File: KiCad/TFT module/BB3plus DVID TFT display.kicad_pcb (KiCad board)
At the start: 2 copper layers, 136 x 92 mm, 66 parts, among them IC1 TFP401APZP, IC2 TCA9554APWR, IC3 TSC2007IPWR, IC4 TPS61169DCKR, SW1 B3FS-4052P, SW2 B3FS-4052P, SW3 B3FS-4052P, SW4 B3FS-4052P, X1 5051102091, X2 F32D-1A7Y1-21040, X3 F3311A7H121006E200

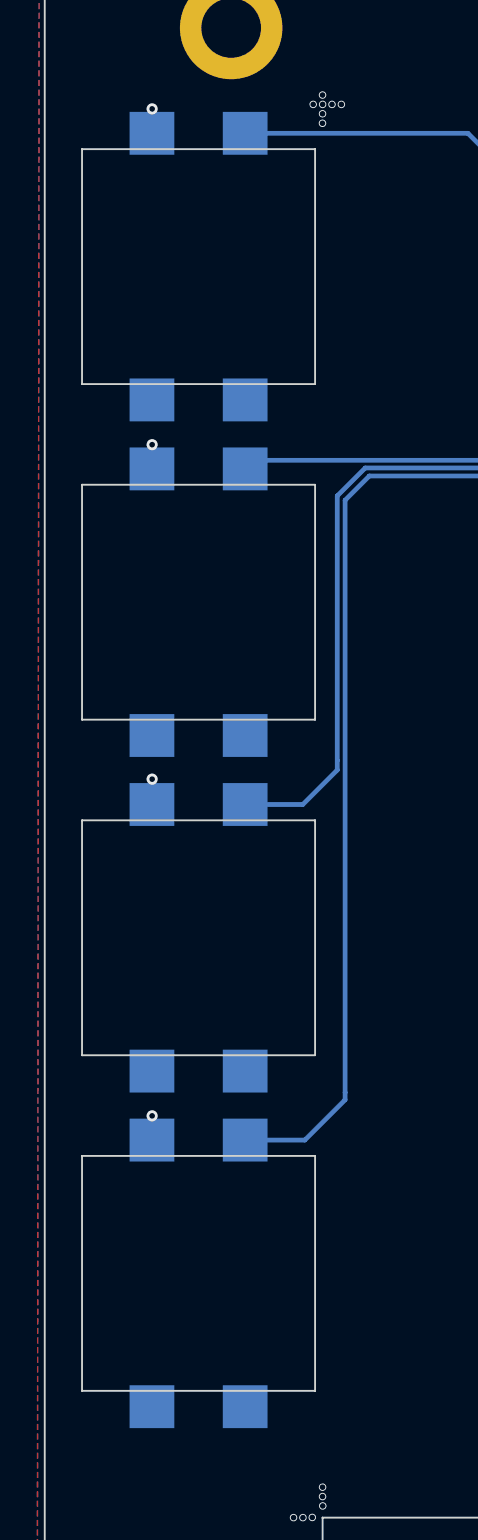
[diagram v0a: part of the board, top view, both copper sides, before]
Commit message: TFT display tactile switches footprint correction
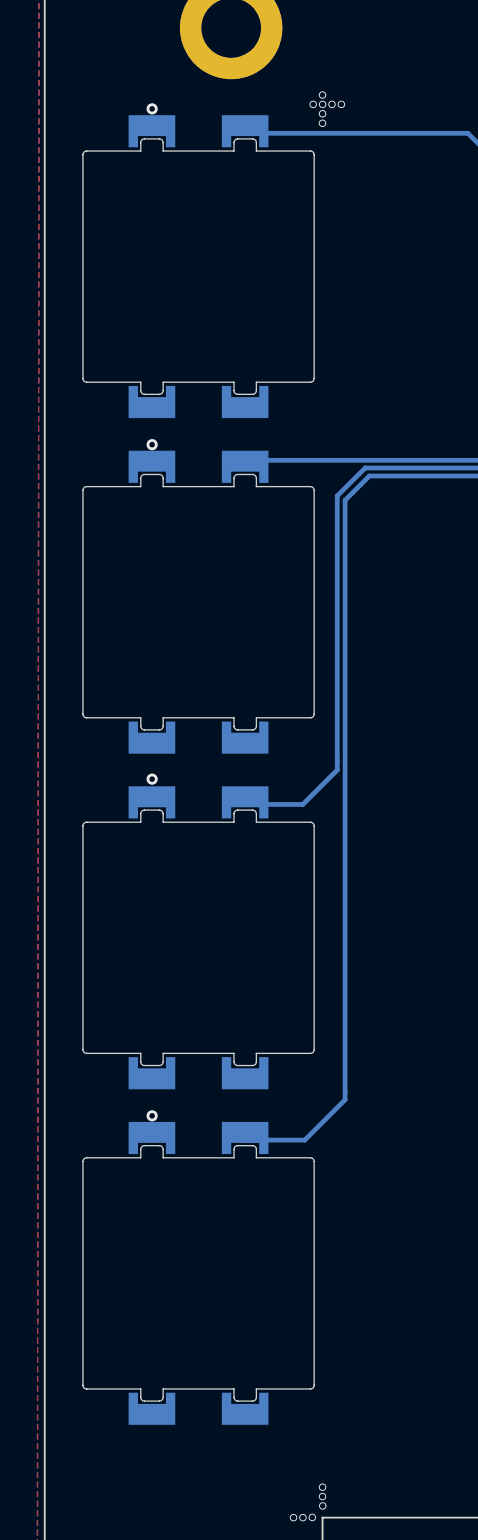
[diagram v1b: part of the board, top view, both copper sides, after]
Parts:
- SW1, SW2, SW3, SW4: footprint PCM_EEZ_unsorted:B3FS-4052P -> PCM_EEZ_unsorted:B3FS-4052P (cut out)
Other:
- outline, holes or cut-outs redrawn
- board text added: "${project_name} (12/2025 ${project_version})"
- board text removed: "${project_name} (11/2025 ${project_version})"

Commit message: Enclosure front and rear panel update, projects location reorganized
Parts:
- X1: value 5051102091 -> 5051102291
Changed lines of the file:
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@@
 			)
 		)
-		(model "${KICAD7_3RD_PARTY}/3dmodels/com_github_eez-open_eez-kicad-libraries/ER-TFT050-6.STEP"
+		(model "${KICAD7_3RD_PARTY}/3dmodels/com_github_eez-open_eez-kicad-libraries/ER-TFT050-6 (simplified).step"
 			(offset
 				(xyz 65.2 42 1)
@@
 			)
 		)
-		(property "Value" "5051102091"
+		(property "Value" "5051102291"
 			(at 0 0 0)
 			(unlocked yes)

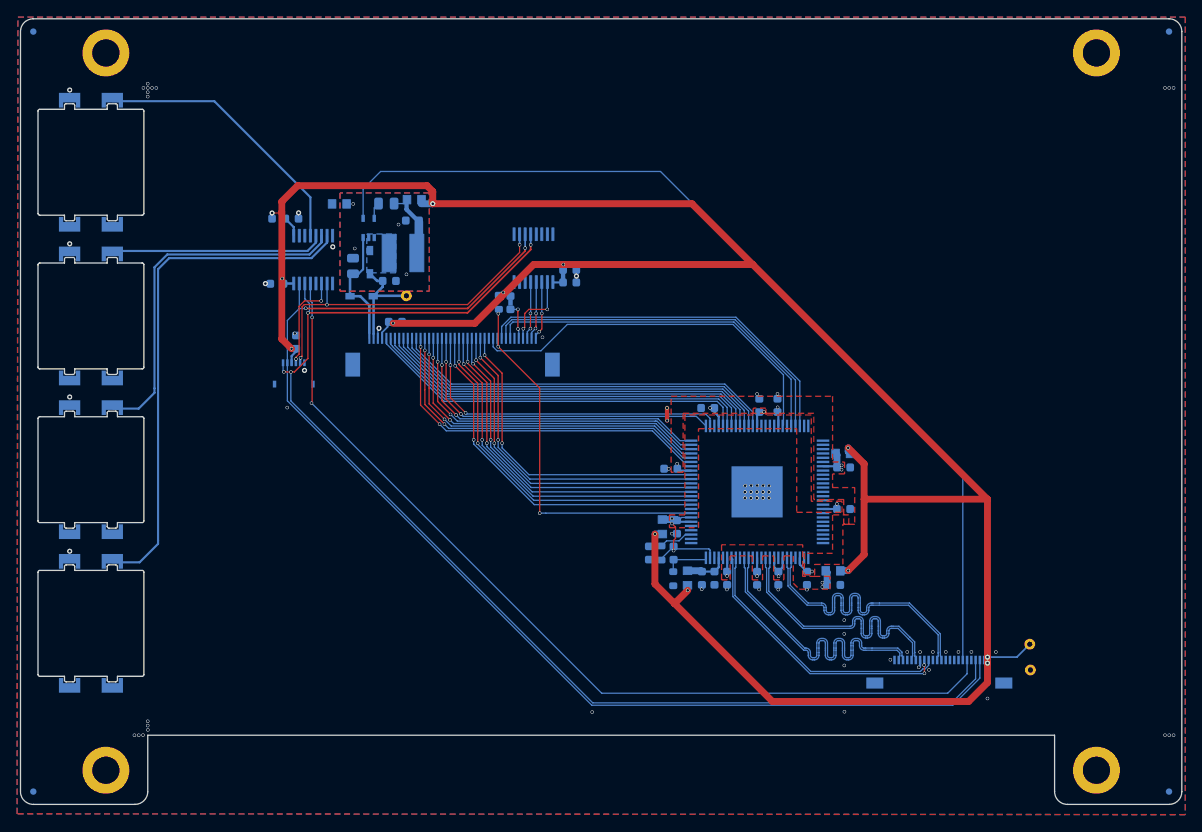
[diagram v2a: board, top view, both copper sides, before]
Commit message: EDID EEPROM added on TFT module
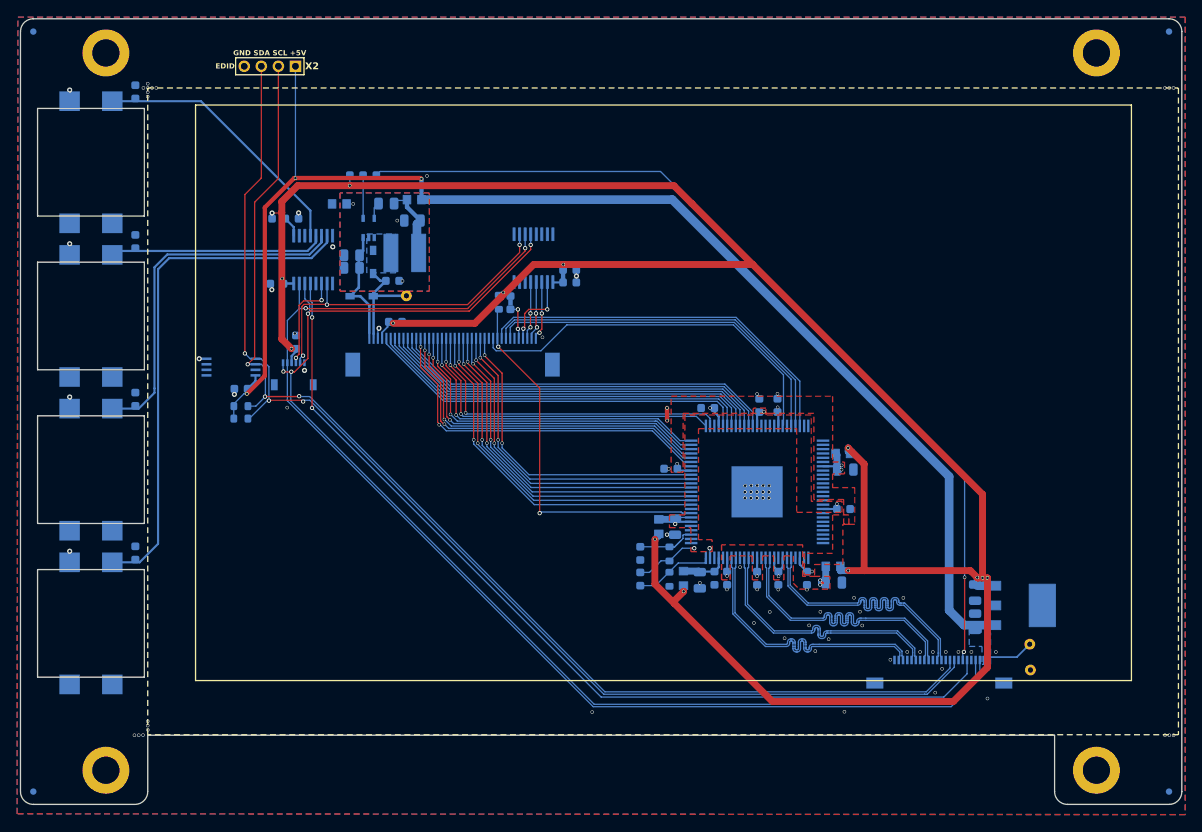
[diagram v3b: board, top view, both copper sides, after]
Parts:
- added C15: 10u, PCM_EEZ_passives:C_0805_2012Metric, B.Cu at (196.8, 120.1)
- added C16: 100n, PCM_EEZ_passives:C_0603_1608Metric, B.Cu at (110.8, 92.8)
- added C19: 10u, PCM_EEZ_passives:C_0805_2012Metric, B.Cu at (196.8, 116.7)
- added C22: 10n, PCM_EEZ_passives:C_0603_1608Metric, B.Cu at (98.5, 112.1)
- added C24: 10n, PCM_EEZ_passives:C_0603_1608Metric, B.Cu at (98.5, 94.0)
- added C25: 10n, PCM_EEZ_passives:C_0603_1608Metric, B.Cu at (98.5, 58.1)
- added C26: 10n, PCM_EEZ_passives:C_0603_1608Metric, B.Cu at (98.5, 75.6)
- added IC2: M24C04-RDW6TP, PCM_EEZ_SMD:TSSOP-8, B.Cu at (109.6, 90.3)
- added IC3: AZ1117CH2-3.3TRG1, PCM_EEZ_SMD:SOT223, B.Cu at (202.1, 118.2)
- added JP5: 0R, PCM_EEZ_SMD:JP3 shorted with 0R (0603), B.Cu at (125.9, 67.8)
- added R3: 10K, PCM_EEZ_passives:R_0603_1608Metric, B.Cu at (110.8, 94.9)
- added R4: 10K, PCM_EEZ_passives:R_0603_1608Metric, B.Cu at (110.8, 96.3)
- added R8: 9R1, Resistor_SMD:R_0805_2012Metric, B.Cu at (123.8, 78.7)
- added X2: M22-2010446, PCM_EEZ_connectors:M22-2010446, F.Cu at (114.2, 55.1)
- C1, C2, C3, C4: footprint PCM_EEZ_passives:C_0603_1608Metric -> PCM_EEZ_passives:C_0805_2012Metric
- C21: renamed from C18; footprint PCM_EEZ_passives:C_0603_1608Metric -> PCM_EEZ_passives:C_0805_2012Metric
- JP4: value ~ -> 0R
- SW1, SW2, SW3, SW4: footprint PCM_EEZ_unsorted:B3FS-4052P (cut out) -> PCM_EEZ_unsorted:B3FS-4052P
- X1: value 5051102291 -> 5051102091
- moved JP1 4.94 mm to (157.6, 115.1)
- moved R7 1.26 mm to (123.8, 77.2), turned to 0 degrees
- moved JP2 1.02 mm to (157.6, 112.1)
- moved R1 0.95 mm to (161.0, 112.2)
- moved FB3 0.53 mm to (180.2, 113.6)
- moved FB4 0.47 mm to (162.6, 115.0)
- moved R2 0.44 mm to (161.0, 115.1)
- moved FB1 0.42 mm to (159.8, 109.0)
- moved C28 0.37 mm to (128.6, 80.2)
- moved D1 0.37 mm to (126.3, 78.0)
- moved C4 0.35 mm to (164.6, 115.2)
- moved C2 0.32 mm to (181.6, 102.3)
- moved C3 0.28 mm to (180.2, 115.5)
- moved C1 0.24 mm to (161.7, 109.0)
- moved L1 0.21 mm to (130.0, 76.9)
- renumbered C15 to C17, C16 to C18, C17 to C20, C19 to C23, C20 to C27, C21 to C28, FM3 to FM2, FM2 to FM3, IC2 to IC4, IC3 to IC5, IC4 to IC6, R3 to R5, R4 to R6, R5 to R7, TP2 to TP1, TP1 to TP2, X2 to X3, X3 to X4
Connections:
- FB5 pad 1: +3V3 -> +5V
- IC6 pad 4: /BL_PWM -> Net-(IC6-CTRL)
- TP2 pad 1: +3V3 -> +5V
- X1 pad 1: +3V3 -> +5V
- X1 pad 14: /DSI_CLK_P -> /DSI_D1_P
- X1 pad 15: /DSI_CLK_N -> /DSI_D1_N
- X1 pad 17: /DSI_D1_P -> /DSI_D0_P
- X1 pad 18: /DSI_D1_N -> /DSI_D0_N
- X1 pad 20: /DSI_D0_P -> /DSI_CLK_P
- X1 pad 21: /DSI_D0_N -> /DSI_CLK_N
- X1 pad 8: unconnected-(X1-DPHY_D3_P-Pad8) -> /EDID_SDA
- X1 pad 9: unconnected-(X1-DPHY_D3_N-Pad9) -> /EDID_SCL
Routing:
- net +5V: track 0.00 -> 165.8 mm, vias 0 -> 3
- net /EDID_SDA: track 0.00 -> 142.1 mm, vias 0 -> 3
- net /EDID_SCL: track 0.00 -> 141.2 mm, vias 0 -> 3
- net /DSI_D0_N: track 36.9 -> 30.5 mm
- net /DSI_D0_P: track 36.9 -> 30.5 mm
- net /BL_PWM: track 111.0 -> 105.5 mm, vias 0 -> 2
- net Net-(IC6-CTRL): track 0.00 -> 5.04 mm
- net Net-(IC1-OCK_INV): track 5.42 -> 9.59 mm
- net +3V3: track 288.2 -> 284.7 mm, vias 13 -> 14
- net Net-(IC1-ST): track 5.51 -> 8.39 mm
- net /VDDIO: track 20.1 -> 17.5 mm
- net /DSI_D2_N: track 35.3 -> 33.0 mm
- net /DSI_D2_P: track 35.3 -> 33.0 mm
- net /DSI_CLK_P: track 31.7 -> 32.9 mm
- net GND: track 3.63 -> 2.70 mm, vias 74 -> 86
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- added copper zone on B.Cu, net +5V
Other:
- outline, holes or cut-outs redrawn
- board text added: "+5V SCL SDA GND"
- board text added: "EDID"
- board text added: "GND SDA SCL +5V"

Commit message: Tactile switches footprint update
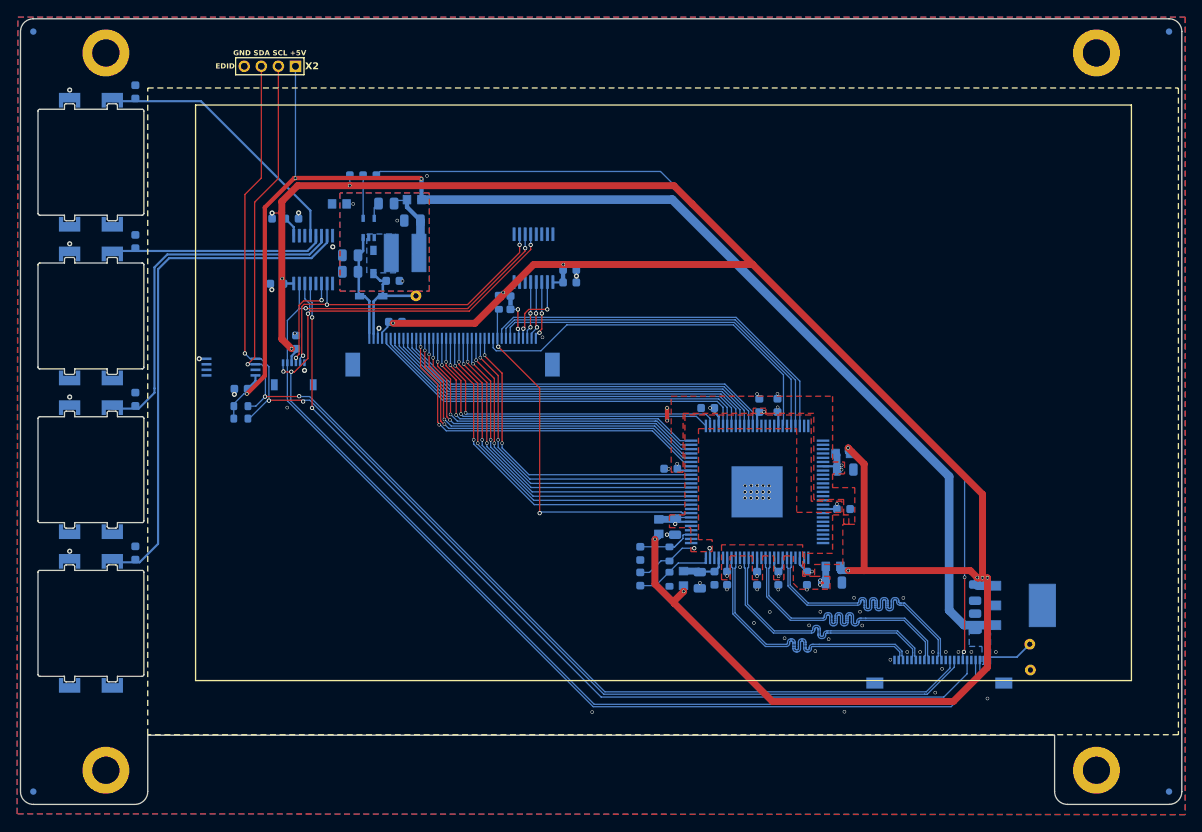
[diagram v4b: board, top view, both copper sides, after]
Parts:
- R6, R7, R8: footprint Resistor_SMD:R_0805_2012Metric -> PCM_EEZ_passives:R_0805_2012Metric
- SW1, SW2, SW3, SW4: footprint PCM_EEZ_unsorted:B3FS-4052P -> PCM_EEZ_unsorted:B3FS-4052P (cut out)
- moved TP3 1.12 mm to (131.3, 81.9)
- moved ZD1 1.12 mm to (126.1, 82.0)
- moved R8 0.50 mm to (123.6, 79.1)
- moved R7 0.18 mm to (123.6, 77.2)
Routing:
- net /VLED-: track 14.1 -> 12.9 mm
- net GND: vias 86 -> 67
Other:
- outline, holes or cut-outs redrawn

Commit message: #2
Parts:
- moved TP2 32.2 mm to (174.2, 108.7)
- moved TP1 28.2 mm to (180.8, 108.7)
- moved IC3 24.9 mm to (181.4, 104.4)
- moved C15 24.9 mm to (176.1, 106.3)
- moved C19 24.9 mm to (176.1, 102.9)
- moved X1 16.5 mm to (178.6, 118.3), turned to -90 degrees
- moved C13 13.4 mm to (154.3, 115.0)
- moved C4 13.4 mm to (151.1, 115.2)
- moved C8 13.4 mm to (152.8, 115.0)
- moved R1 13.4 mm to (147.6, 112.2)
- moved R2 13.4 mm to (147.6, 115.1)
- moved FB4 13.4 mm to (149.2, 115.0)
- moved C1 13.3 mm to (148.3, 109.0)
- moved C10 13.3 mm to (160.3, 94.8)
- moved C11 13.3 mm to (157.9, 115.0)
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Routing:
- net +3V3: track 284.7 -> 234.6 mm
- net /SDA: track 145.0 -> 96.6 mm, vias 2 -> 3
- net /SCL: track 146.3 -> 99.7 mm
- net +5V: track 165.8 -> 136.1 mm
- net /BL_PWM: track 105.5 -> 80.8 mm
- net /DPI_PCLK: track 44.9 -> 29.5 mm
- net /DPI_DE: track 42.6 -> 27.7 mm
- net /DPI_VSYNC: track 43.8 -> 29.9 mm
- net /DPI_HSYNC: track 44.9 -> 31.0 mm
- net /QE15: track 39.2 -> 25.8 mm
- net /QE16: track 45.3 -> 32.0 mm
- net /QE23: track 45.3 -> 32.0 mm
- net /QE22: track 45.4 -> 32.0 mm
- net /QE21: track 45.3 -> 32.0 mm
- net /QE20: track 45.4 -> 32.0 mm
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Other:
- board text added: "${project_name} (02/2026 ${project_version})"
- board text removed: "${project_name} (12/2025 ${project_version})"
- board text removed: "Designed and manufactured in Croatia"

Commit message: #1, #3, #4
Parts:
- added IC5: TPS2069E, PCM_EEZ_SMD:DBV5, B.Cu at (150.0, 82.8)
- moved C25 1.06 mm to (150.1, 79.7), turned to 90 degrees
- moved C24 1.01 mm to (148.6, 79.7), turned to 90 degrees
- renumbered C15 to C1, C24 to C10, C1 to C11, C5 to C12, C9 to C13, C22 to C14, C2 to C15, C6 to C16, C10 to C17, C12 to C18, C14 to C19, C19 to C2, C3 to C20, C7 to C21, C11 to C22, C13 to C23, C23 to C24, C27 to C25, C4 to C26, C8 to C27, C16 to C28, C28 to C3, C21 to C4, C17 to C5, C25 to C6, C26 to C7, C18 to C8, C20 to C9, FB5 to FB1, FB6 to FB2, FB1 to FB3, FB2 to FB4, FB3 to FB5, FB4 to FB6, FM3 to FM2, FM2 to FM3, IC3 to IC2, IC6 to IC3, IC5 to IC6, IC2 to IC7, JP5 to JP1, JP1 to JP3, JP3 to JP5, R6 to R1, R7 to R2, R8 to R3, R1 to R4, R2 to R5, R5 to R6, R3 to R7, R4 to R8, TP2 to TP1, TP3 to TP2, TP1 to TP3, X4 to X2, X2 to X4
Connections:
- C24 pad 1: +3V3 -> Net-(IC5-OUT)
- C25 pad 1: +3V3 -> Net-(IC5-OUT)
- IC4 pad 12: unconnected-(IC4-P7-Pad12) -> /TOUCH_EN
- IC6 pad 1: +3V3 -> Net-(IC5-OUT)
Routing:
- net /TOUCH_EN: track 0.00 -> 34.2 mm, vias 0 -> 2
- net +3V3: track 234.6 -> 229.0 mm
- net Net-(IC5-OUT): track 0.00 -> 4.59 mm
- net GND: vias 64 -> 65

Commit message: #7
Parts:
- added JP5: 0R, PCM_EEZ_SMD:JP3 shorted (0603), B.Cu at (116.8, 71.1)
- H1, H2, H3, H4: value MountingHole_Pad -> ~
- JP4: footprint PCM_EEZ_SMD:JP3 shorted with 0R (0603) 2-3 -> PCM_EEZ_SMD:JP3 shorted (0603)
- moved JP4 1.51 mm to (115.3, 72.9), turned to 180 degrees
- renumbered JP5 to JP6
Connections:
- IC4 pad 2: GND -> Net-(IC4-A1)
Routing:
- net Net-(IC4-A1): track 0.00 -> 8.21 mm
- net +3V3: track 229.0 -> 230.3 mm
- net Net-(IC4-P0): track 31.4 -> 32.5 mm
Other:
- board text added: "${project_name} (05/2026 ${project_version})"
- board text removed: "${project_name} (02/2026 ${project_version})"
